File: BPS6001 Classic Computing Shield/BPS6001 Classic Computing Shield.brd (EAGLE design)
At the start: 119.4 x 58.7 mm, 85 parts, among them IC1 MAX3232CSE, X1 VGA

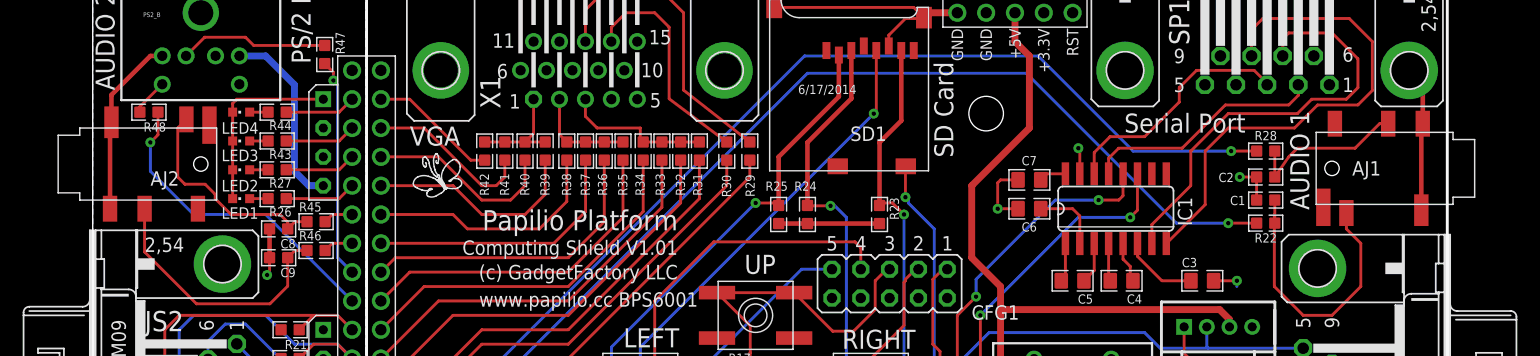
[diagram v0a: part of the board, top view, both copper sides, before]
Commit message: Fix Audio Jack.
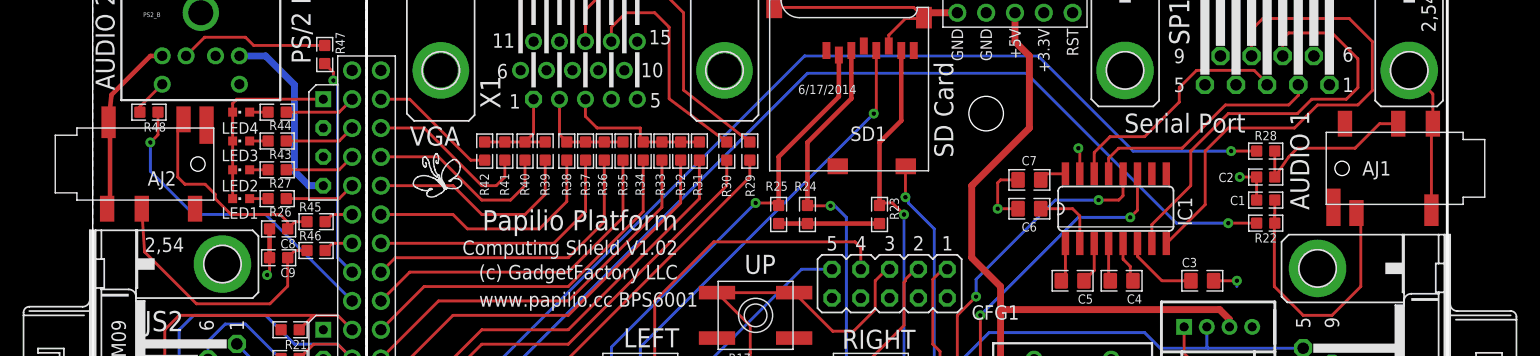
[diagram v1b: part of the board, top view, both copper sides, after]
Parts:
- moved AJ1 0.89 mm to (115.7, 39.6)
- moved AJ2 0.25 mm to (3.68, 40.0)
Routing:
- net N$34: track 14.4 -> 15.3 mm
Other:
- board text added: "Computing Shield V1.02"
- board text removed: "Computing Shield V1.01"
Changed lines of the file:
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@@
 <wire x1="119.38" y1="55.88" x2="119.38" y2="0" width="0.254" layer="20"/>
 <text x="51.562" y="35.941" size="1.778" layer="21" ratio="12" rot="R180">Papilio Platform</text>
-<text x="51.562" y="33.274" size="1.27" layer="21" ratio="10" rot="R180">Computing Shield V1.01</text>
+<text x="51.562" y="33.274" size="1.27" layer="21" ratio="10" rot="R180">Computing Shield V1.02</text>
 <text x="94.742" y="19.05" size="1.6764" layer="21" ratio="15" rot="R270">PS/2 A</text>
 <text x="15.621" y="2.54" size="1.6764" layer="21" ratio="15" rot="R180">Joystick 2</text>
@@
 <attribute name="PARTNO" value="RMCF0603JT47K0" x="17.399" y="25.4" size="1.778" layer="27" rot="R180" display="off"/>
 </element>
-<element name="AJ1" library="OPL Eagle Library" package="6P-SMD-3.5" value="AUDIO-CONNECTOR-6P-SMD-3440030P1" x="114.808" y="39.624" smashed="yes">
-<attribute name="NAME" x="110.998" y="38.989" size="1.27" layer="25" ratio="12"/>
-<attribute name="VALUE" x="110.998" y="39.624" size="0.635" layer="27" ratio="10"/>
-<attribute name="PARTNO" value="3440030P1" x="114.808" y="39.624" size="1.778" layer="27" display="off"/>
+<element name="AJ1" library="OPL Eagle Library" package="6P-SMD-3.5" value="AUDIO-CONNECTOR-6P-SMD-3440030P1" x="115.697" y="39.624" smashed="yes">
+<attribute name="NAME" x="111.887" y="38.989" size="1.27" layer="25" ratio="12"/>
+<attribute name="VALUE" x="111.887" y="39.624" size="0.635" layer="27" ratio="10"/>
+<attribute name="PARTNO" value="3440030P1" x="115.697" y="39.624" size="1.778" layer="27" display="off"/>
 </element>
 <element name="C1" library="GadgetFactory" package="0603" value="4700pF" x="103.378" y="36.83" smashed="yes" rot="R180">
@@
 <attribute name="BOM" value="EXCLUDE" x="20.32" y="21.59" size="1.778" layer="27" display="off"/>
 </element>
-<element name="AJ2" library="OPL Eagle Library" package="6P-SMD-3.5" value="AUDIO-CONNECTOR-6P-SMD-3440030P1" x="3.937" y="40.005" smashed="yes" rot="R180">
-<attribute name="NAME" x="7.62" y="39.37" size="1.27" layer="25" ratio="12" rot="R180"/>
-<attribute name="VALUE" x="7.747" y="40.005" size="0.635" layer="27" ratio="10" rot="R180"/>
-<attribute name="PARTNO" value="3440030P1" x="3.937" y="40.005" size="1.778" layer="27" rot="R180" display="off"/>
+<element name="AJ2" library="OPL Eagle Library" package="6P-SMD-3.5" value="AUDIO-CONNECTOR-6P-SMD-3440030P1" x="3.683" y="40.005" smashed="yes" rot="R180">
+<attribute name="NAME" x="7.366" y="39.37" size="1.27" layer="25" ratio="12" rot="R180"/>
+<attribute name="VALUE" x="7.493" y="40.005" size="0.635" layer="27" ratio="10" rot="R180"/>
+<attribute name="PARTNO" value="3440030P1" x="3.683" y="40.005" size="1.778" layer="27" rot="R180" display="off"/>
 </element>
 <element name="C8" library="GadgetFactory" package="0603" value="4700pF" x="16.383" y="34.29" rot="R180">
@@
 <wire x1="71.628" y1="52.832" x2="73.182" y2="52.832" width="0.254" layer="1"/>
 <wire x1="73.182" y1="52.832" x2="73.26" y2="52.91" width="0.254" layer="1"/>
-<wire x1="117.094" y1="35.941" x2="117.094" y2="43.434" width="0.4064" layer="1"/>
-<wire x1="117.094" y1="43.434" x2="117.221" y2="43.561" width="0.4064" layer="1"/>
-<wire x1="117.221" y1="43.561" x2="117.221" y2="47.0662" width="0.4064" layer="1"/>
-<wire x1="117.221" y1="47.0662" x2="116.0272" y2="48.26" width="0.4064" layer="1"/>
 <wire x1="70.32" y1="15.875" x2="69.469" y2="15.875" width="0.254" layer="1"/>
 <wire x1="69.469" y1="15.875" x2="68.453" y2="14.859" width="0.254" layer="1"/>
@@
 <contactref element="PS2_A" pad="3"/>
 <contactref element="PS2_A" pad="3"/>
+<wire x1="118.11" y1="43.561" x2="118.11" y2="46.1772" width="0.254" layer="1"/>
+<wire x1="118.11" y1="46.1772" x2="116.0272" y2="48.26" width="0.254" layer="1"/>
+<wire x1="117.983" y1="35.941" x2="117.983" y2="43.434" width="0.254" layer="1"/>
+<wire x1="117.983" y1="43.434" x2="118.11" y2="43.561" width="0.254" layer="1"/>
 </signal>
 <signal name="HORIZONTAL_SYNC">
@@
 <contactref element="AJ2" pad="COM1"/>
 <wire x1="15.583" y1="31.75" x2="15.583" y2="34.29" width="0.4064" layer="1"/>
-<wire x1="1.524" y1="36.068" x2="1.524" y2="43.561" width="0.4064" layer="1"/>
-<wire x1="1.524" y1="43.561" x2="1.651" y2="43.688" width="0.4064" layer="1"/>
-<wire x1="1.651" y1="43.688" x2="1.651" y2="46.101" width="0.4064" layer="1"/>
+<wire x1="1.524" y1="43.561" x2="1.397" y2="43.688" width="0.4064" layer="1"/>
+<wire x1="1.397" y1="43.688" x2="1.651" y2="46.101" width="0.4064" layer="1"/>
 <contactref element="PS2_B" pad="3"/>
 <wire x1="1.651" y1="46.101" x2="5.08" y2="49.53" width="0.4064" layer="1"/>
 <wire x1="5.08" y1="49.53" x2="6.116" y2="49.53" width="0.4064" layer="1"/>
 <wire x1="6.116" y1="49.53" x2="6.125" y2="49.539" width="0.4064" layer="1"/>
+<wire x1="1.524" y1="43.561" x2="1.524" y2="36.322" width="0.4064" layer="1"/>
+<wire x1="1.524" y1="36.322" x2="1.27" y2="36.068" width="0.4064" layer="1"/>
 </signal>
 <signal name="AUDIO1-LEFT">
@@
 <contactref element="AJ1" pad="L"/>
 <wire x1="104.178" y1="36.83" x2="104.178" y2="34.798" width="0.254" layer="1"/>
-<wire x1="110.49" y1="35.687" x2="110.49" y2="34.29" width="0.254" layer="1"/>
-<wire x1="110.49" y1="34.29" x2="111.76" y2="33.02" width="0.254" layer="1"/>
-<wire x1="111.76" y1="33.02" x2="111.76" y2="29.21" width="0.254" layer="1"/>
+<wire x1="111.76" y1="35.306" x2="111.76" y2="29.21" width="0.254" layer="1"/>
 <wire x1="111.76" y1="29.21" x2="109.22" y2="26.67" width="0.254" layer="1"/>
 <wire x1="109.22" y1="26.67" x2="106.68" y2="26.67" width="0.254" layer="1"/>
@@
 <wire x1="104.14" y1="29.21" x2="104.14" y2="35.522" width="0.254" layer="1"/>
 <wire x1="104.14" y1="35.522" x2="104.178" y2="34.798" width="0.254" layer="1"/>
+<wire x1="111.76" y1="35.306" x2="111.379" y2="35.687" width="0.254" layer="1"/>
 </signal>
 <signal name="N$34">
@@
 <contactref element="AJ1" pad="R"/>
 <wire x1="104.178" y1="41.148" x2="104.178" y2="38.862" width="0.254" layer="1"/>
-<wire x1="114.173" y1="43.561" x2="113.411" y2="43.561" width="0.254" layer="1"/>
+<wire x1="115.062" y1="43.561" x2="113.411" y2="43.561" width="0.254" layer="1"/>
 <wire x1="113.411" y1="43.561" x2="111.252" y2="41.402" width="0.254" layer="1"/>
 <wire x1="111.252" y1="41.402" x2="106.172" y2="41.402" width="0.254" layer="1"/>
@@
 <wire x1="8.128" y1="38.227" x2="7.493" y2="38.862" width="0.254" layer="1"/>
 <wire x1="7.493" y1="38.862" x2="7.493" y2="43.18" width="0.254" layer="1"/>
-<wire x1="7.493" y1="43.18" x2="8.255" y2="43.942" width="0.254" layer="1"/>
+<wire x1="7.493" y1="43.18" x2="8.001" y2="43.942" width="0.254" layer="1"/>
 </signal>
 <signal name="N$15">
@@
 <wire x1="15.621" y1="27.686" x2="9.144" y2="27.686" width="0.254" layer="1"/>
 <wire x1="9.144" y1="27.686" x2="4.572" y2="32.258" width="0.254" layer="1"/>
-<wire x1="4.572" y1="32.258" x2="4.572" y2="36.068" width="0.254" layer="1"/>
+<wire x1="4.572" y1="32.258" x2="4.318" y2="36.068" width="0.254" layer="1"/>
 </signal>
 <signal name="AUDIO2-LEFT">
